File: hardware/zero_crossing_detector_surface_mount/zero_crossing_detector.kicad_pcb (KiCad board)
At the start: 2 copper layers, 93 x 61 mm, 85 parts, among them J1 Conn_01x02, J2 BOOT0, J3 Conn_02x14_Odd_Even, J4 USB_B_Micro, J5 PowerSelect, J6 K-Type, J7 BOOT1, Q1 2N3904, SW1 Reset, U1 EL357N(C)(TA)-G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

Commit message: Added open hardware logo to PCB. Fixed some doc typos
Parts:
- added REF**: OSHW-Symbol_6.7x6mm_SilkScreen, Symbol:OSHW-Symbol_6.7x6mm_SilkScreen, B.Cu at (204.2, 55.9)
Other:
- board text added: "open hardware open software"

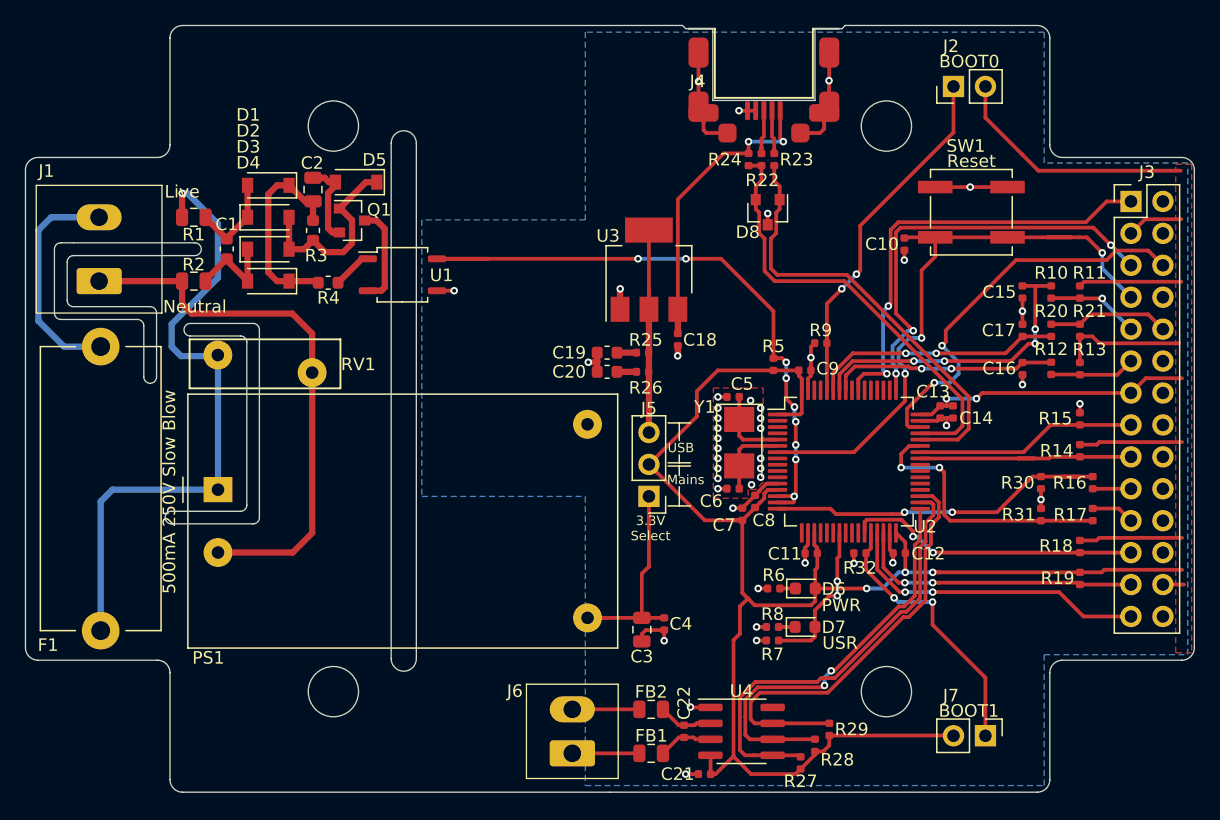
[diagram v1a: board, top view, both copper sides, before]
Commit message: Changed to 5v AC-DC module. Added transistor to drive SSR output. Updated LDO
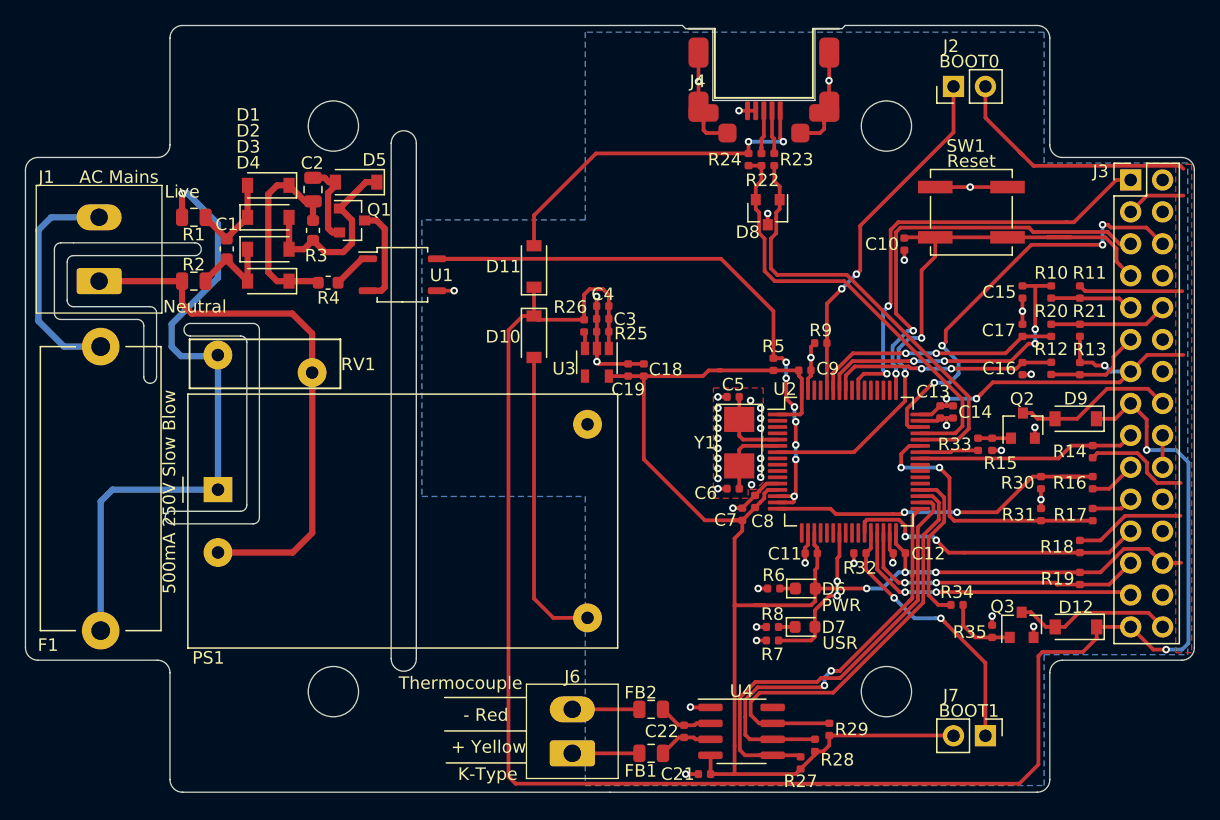
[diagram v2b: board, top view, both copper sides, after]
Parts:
- removed C20: 22uF, Capacitor_SMD:C_0603_1608Metric
- removed J5: PowerSelect, Connector_PinHeader_2.54mm:PinHeader_1x03_P2.54mm_Vertical
- added D10: B5819W, Diode_SMD:D_SOD-123, F.Cu at (204.0, 64.3)
- added D11: B5819W, Diode_SMD:D_SOD-123, F.Cu at (204.0, 58.7)
- added D12: 1N4148, Diode_SMD:D_SOD-123, F.Cu at (247.1, 87.4)
- added D9: 1N4148, Diode_SMD:D_SOD-123, F.Cu at (247.1, 70.8)
- added Q2: 2N3904, Package_TO_SOT_SMD:SOT-23, F.Cu at (242.9, 71.3)
- added Q3: 2N3904, Package_TO_SOT_SMD:SOT-23, F.Cu at (242.8, 87.2)
- added R33: 1k, Resistor_SMD:R_0402_1005Metric, F.Cu at (239.3, 72.8)
- added R34: 1k, Resistor_SMD:R_0402_1005Metric, F.Cu at (237.6, 85.6)
- added R35: 10k, Resistor_SMD:R_0402_1005Metric, F.Cu at (240.4, 87.7)
- C18: value 4.7uf -> 10uF
- C19: value 22uF -> 100nF; footprint Capacitor_SMD:C_0603_1608Metric -> Capacitor_SMD:C_0402_1005Metric
- C3: footprint Capacitor_SMD:C_0805_2012Metric -> Capacitor_SMD:C_0402_1005Metric
- J3: value Conn_02x14_Odd_Even -> Conn_02x15_Odd_Even; footprint Connector_PinHeader_2.54mm:PinHeader_2x14_P2.54mm_Vertical -> Connector_PinHeader_2.54mm:PinHeader_2x15_P2.54mm_Vertical
- PS1: value HLK-PM03 -> HLK-PM01
- R25, R26: value 1 -> 100k
- U3: value AMS1117 -> AP2112K-3.3; footprint Package_TO_SOT_SMD:SOT-223-3_TabPin2 -> Package_TO_SOT_SMD:SOT-23-5
- moved C4 25.8 mm to (209.4, 61.8), turned to 180 degrees
- moved C3 24.9 mm to (209.4, 62.8), turned to 180 degrees
- moved U3 8.45 mm to (209.0, 66.3), turned to 270 degrees
- moved R15 7.27 mm to (240.4, 72.8)
- moved R26 5.92 mm to (207.9, 63.4), turned to 90 degrees
- moved C18 3.63 mm to (212.7, 66.9), turned to 90 degrees
- moved R25 3.58 mm to (209.4, 63.9), turned to 180 degrees
- moved C19 2.17 mm to (211.5, 66.9), turned to 90 degrees
- moved J3 1.71 mm to (251.4, 51.8)
- moved R14 1.02 mm to (248.4, 73.4), turned to 270 degrees
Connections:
- C18 pad 1: /VBUS -> VCC
- C19 pad 1: Net-(C19-Pad1) -> VCC
- C3 pad 1: /3.3V_MAINS -> +5V
- C4 pad 1: /3.3V_MAINS -> +5V
- J3 pad 15: /SSR -> +5V
- J3 pad 16: GND -> /SSR_RAW
- J4 pad 1: /VBUS -> /5V_USB
- PS1 pad 4: /3.3V_MAINS -> /5V_MAINS
- R15 pad 1: /SSR -> GND
- R15 pad 2: GND -> Net-(Q2-Pad1)
- R24 pad 2: /VBUS -> /5V_USB
- R25 pad 1: Net-(C19-Pad1) -> +5V
- R25 pad 2: /3.3V_USB -> GND
- R26 pad 1: Net-(C20-Pad1) -> Net-(R26-Pad1)
- R26 pad 2: /3.3V_USB -> +5V
- U2 pad 36: Net-(U2-Pad36) -> /MISC
- U3 pad 1: GND -> +5V
- U3 pad 2: /3.3V_USB -> GND
- U3 pad 3: /VBUS -> Net-(R26-Pad1)
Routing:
- net +5V: track 0.00 -> 144.6 mm, vias 0 -> 2
- net /5V_USB: track 0.00 -> 27.8 mm, vias 0 -> 2
- net /VBUS: track 24.1 -> 0.00 mm, vias 2 -> 0
- net /5V_MAINS: track 0.00 -> 24.1 mm
- net /3.3V_MAINS: track 17.6 -> 0.00 mm
- net /3.3V_USB: track 16.1 -> 0.00 mm
- net /SSR: track 17.7 -> 4.66 mm
- net /SSR_RAW: track 0.00 -> 12.8 mm
- net /MISC_RAW: track 0.00 -> 12.6 mm
- net /MISC: track 0.00 -> 12.5 mm
- net VCC: track 208.0 -> 217.3 mm, vias 5 -> 6
- net GND: track 63.6 -> 69.4 mm, vias 44 -> 45
- net Net-(Q3-Pad1): track 0.00 -> 5.73 mm
- net Net-(Q2-Pad1): track 0.00 -> 2.62 mm
- net /SWDIO: track 32.2 -> 34.1 mm, vias 2 -> 4
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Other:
- board text added: "+ Yellow"
- board text added: "- Red"
- board text added: "3.3V"
- board text added: "AC Mains"
- board text added: "K-Type"
- board text added: "MISC +"
- board text added: "MISC -"
- board text added: "SSR +"
- board text added: "SSR -"
- board text added: "Thermocouple"
- board text added: "Zero Crossing SSR Controller (SMD) v0.2 oshthings.com/zcssr 13-Nov-19"
- board text removed: "3.3V Select"
- board text removed: "Mains"
- board text removed: "SSR"
- board text removed: "USB"
- board text removed: "Zero Crossing SSR Controller (SMD) v0.2 oshthings.com/zcssr 11-Nov-19"

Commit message: Added some extra silkscreen labels to IO. Fixed image links in project log
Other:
- board text added: "(3.3V)"
- board text added: "(5V)"
- board text added: "(Active LOW)"
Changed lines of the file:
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@@
   (general
     (thickness 1.6)
-    (drawings 141)
+    (drawings 146)
     (tracks 795)
     (zones 0)
@@
     (pad "" np_thru_hole circle (at 0 0) (size 4 4) (drill 4) (layers *.Cu *.Mask))
   )
+  (gr_text "(3.3V)" (at 238.506 84.836) (layer B.SilkS)
+    (effects (font (size 0.75 0.75) (thickness 0.1)) (justify left mirror))
+  )
+  (gr_text "(3.3V)" (at 238.506 82.296) (layer B.SilkS)
+    (effects (font (size 0.75 0.75) (thickness 0.1)) (justify left mirror))
+  )
+  (gr_text "(Active LOW)" (at 238.506 72.136) (layer B.SilkS)
+    (effects (font (size 0.75 0.75) (thickness 0.1)) (justify left mirror))
+  )
+  (gr_text "(5V)" (at 238.506 69.596) (layer B.SilkS)
+    (effects (font (size 0.75 0.75) (thickness 0.1)) (justify left mirror))
+  )
+  (gr_text "(5V)" (at 238.506 87.376) (layer B.SilkS)
+    (effects (font (size 0.75 0.75) (thickness 0.1)) (justify left mirror))
+  )
   (gr_text "AC Mains" (at 170.942 51.562) (layer F.SilkS)

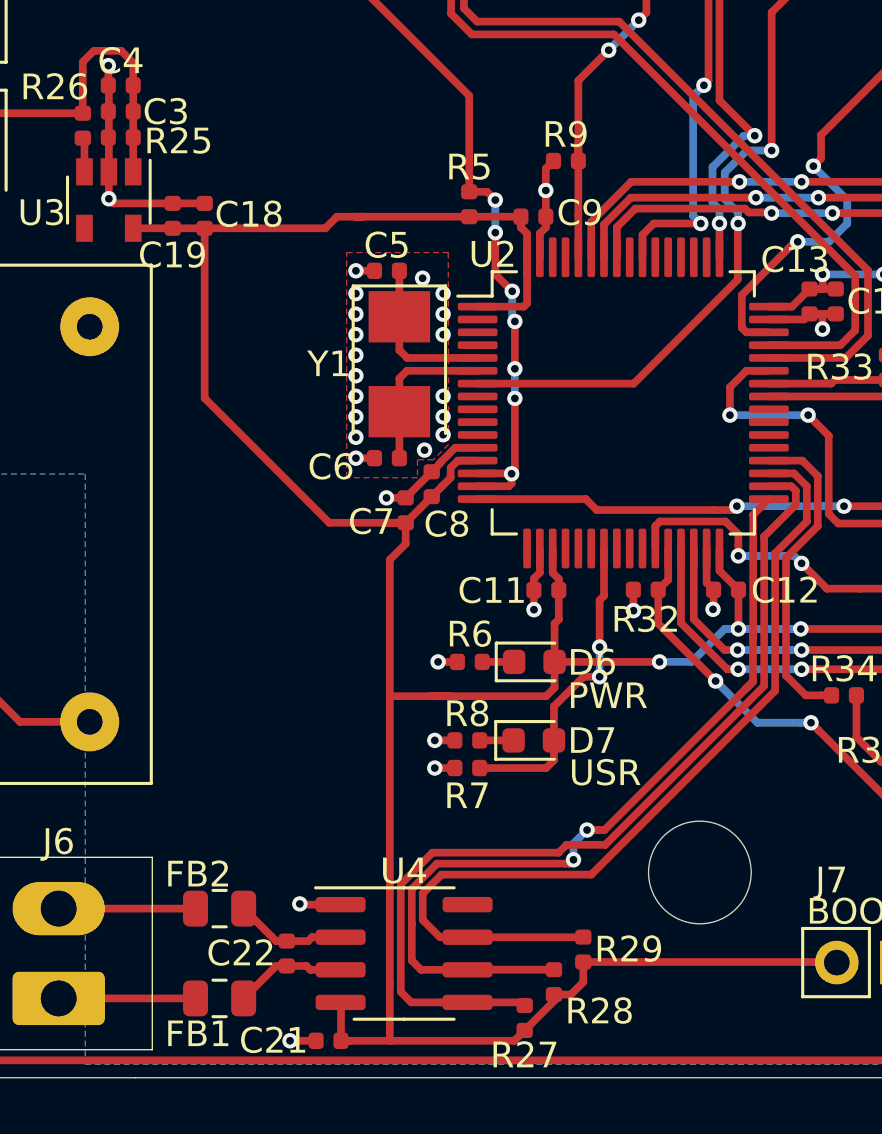
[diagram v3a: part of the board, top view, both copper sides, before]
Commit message: Added tiny 1x1mm RGB LED to pcb
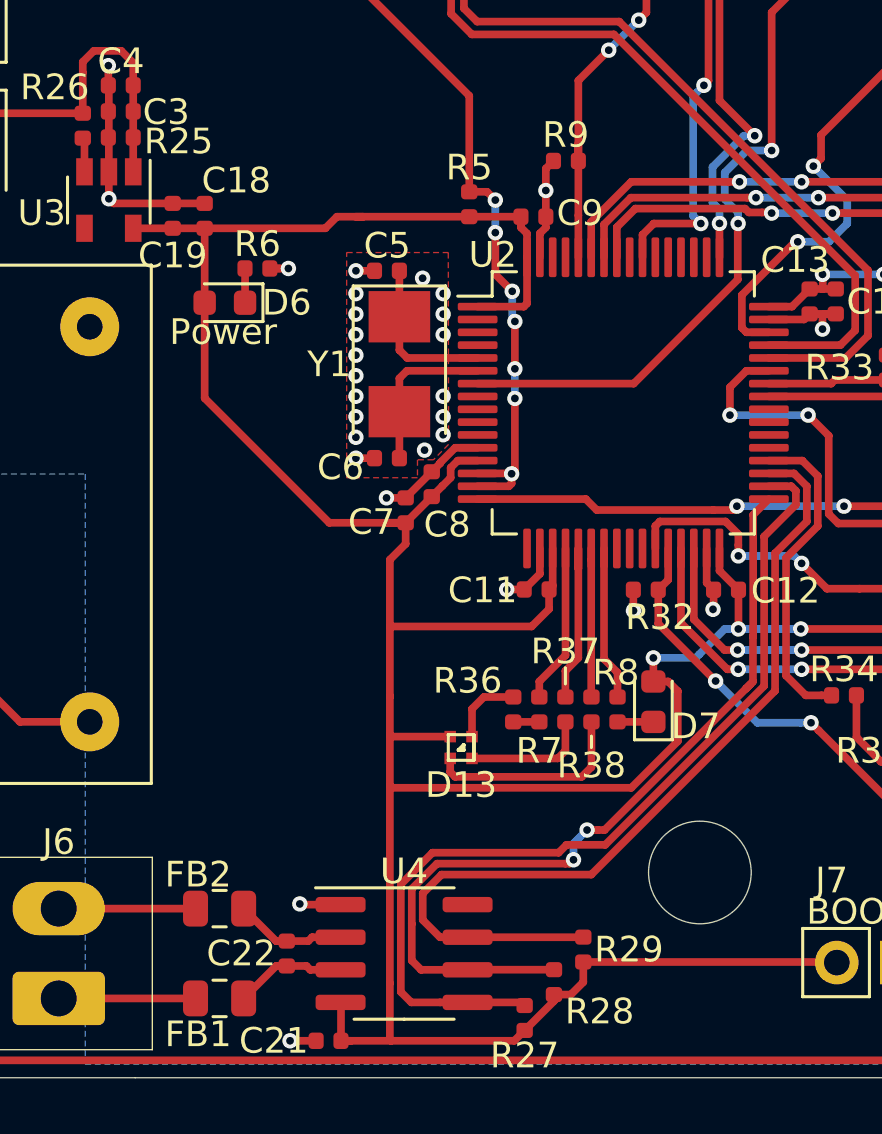
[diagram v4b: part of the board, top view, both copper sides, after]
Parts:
- added D13: LED_ARBG, Custom:SMLP34RGB, F.Cu at (222.7, 87.6)
- added R36: 220, Resistor_SMD:R_0402_1005Metric, F.Cu at (224.7, 86.1)
- added R37: 75, Resistor_SMD:R_0402_1005Metric, F.Cu at (226.8, 86.1)
- added R38: 47, Resistor_SMD:R_0402_1005Metric, F.Cu at (227.8, 86.1)
- R7: value 10k -> 33
- R8: value 150 -> 220
- moved D6 18.5 mm to (213.5, 70.3), turned to 180 degrees
- moved R6 17.4 mm to (214.8, 69.0), turned to 0 degrees
- moved R8 5.98 mm to (228.8, 86.1), turned to 90 degrees
- moved D7 4.90 mm to (230.2, 85.8), turned to 90 degrees
- moved R7 3.62 mm to (225.7, 86.1), turned to 90 degrees
- moved C11 0.38 mm to (225.6, 81.5)
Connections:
- D7 pad 2: /USR_LED -> VCC
- R7 pad 1: /USR_LED -> Net-(R36-Pad2)
- R7 pad 2: GND -> /R_LED
- R8 pad 2: GND -> /USR_LED
- U2 pad 20: Net-(U2-Pad20) -> /R_LED
- U2 pad 21: Net-(U2-Pad21) -> /B_LED
- U2 pad 22: Net-(U2-Pad22) -> /G_LED
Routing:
- net VCC: track 217.3 -> 227.5 mm
- net Net-(D13-Pad4): track 0.00 -> 8.03 mm
- net /B_LED: track 0.00 -> 6.77 mm
- net /USR_LED: track 12.4 -> 6.01 mm, vias 2 -> 0
- net /R_LED: track 0.00 -> 6.21 mm
- net /G_LED: track 0.00 -> 5.79 mm
- net Net-(D13-Pad3): track 0.00 -> 4.89 mm
- net Net-(D13-Pad2): track 0.00 -> 2.88 mm
- net GND: track 69.4 -> 68.3 mm, vias 45 -> 43
- net Net-(R36-Pad2): track 0.00 -> 1.02 mm
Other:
- board text added: "Power"
- board text added: "Zero Crossing SSR Controller (SMD) v0.2 oshthings.com/zcssr 15-Nov-19"
- board text removed: "PWR"
- board text removed: "USR"
- board text removed: "Zero Crossing SSR Controller (SMD) v0.2 oshthings.com/zcssr 13-Nov-19"

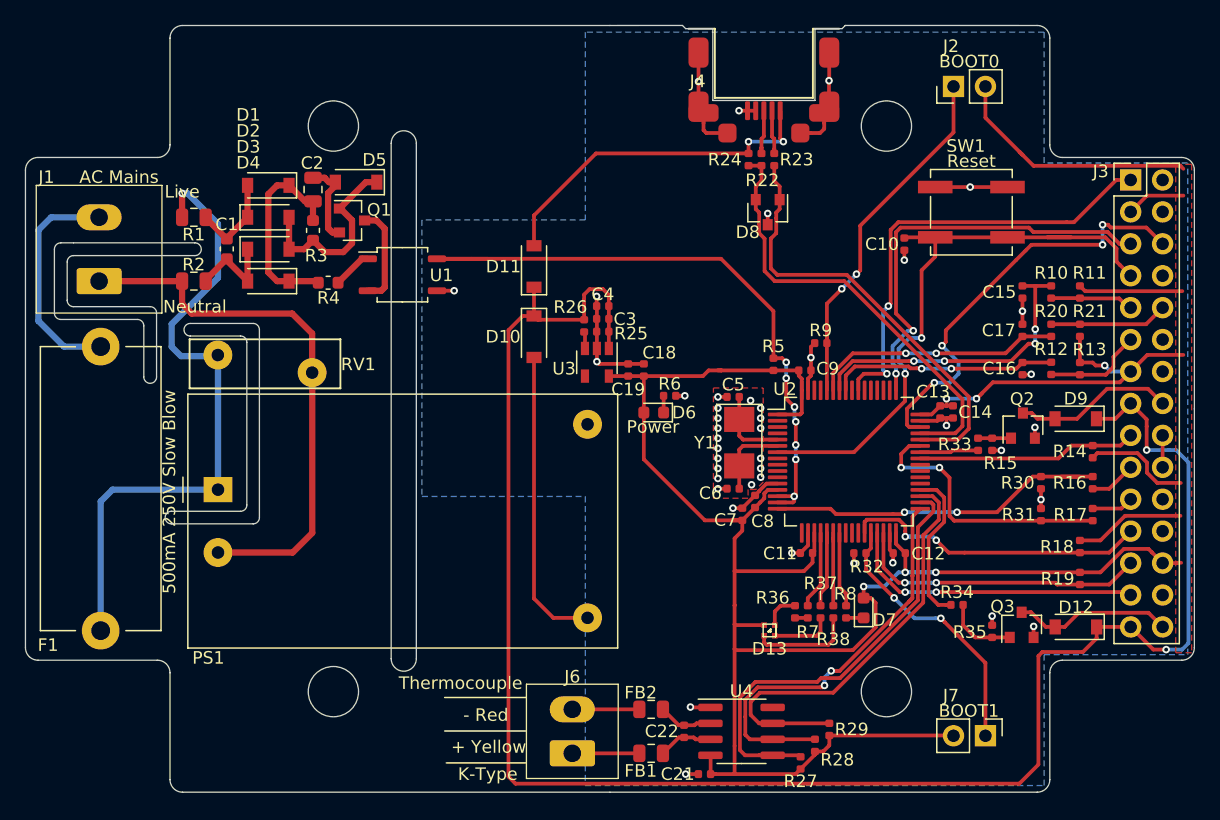
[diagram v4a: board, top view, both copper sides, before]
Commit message: Switched USB ESD diode for STM recommened one. Added GND plane around USB traces on top layer
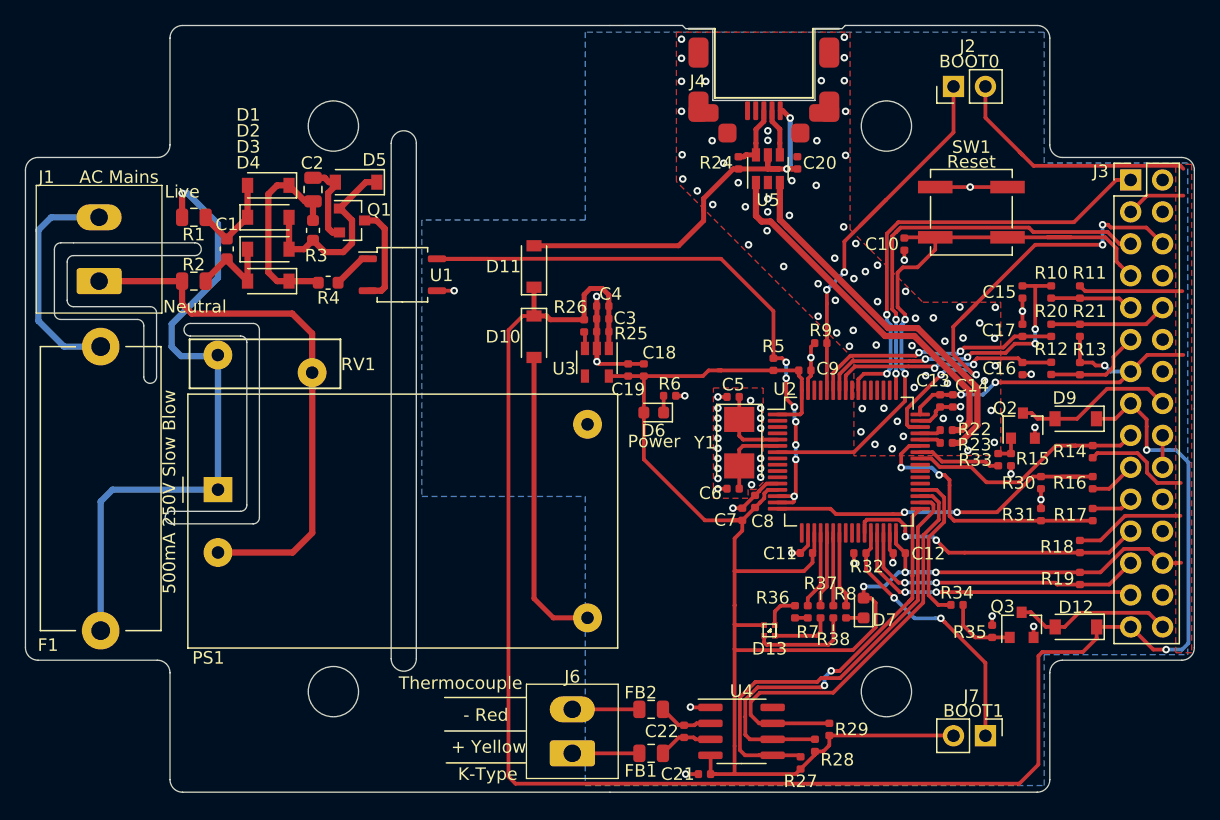
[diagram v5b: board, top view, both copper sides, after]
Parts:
- removed D8: CESD5V0AP, Package_TO_SOT_SMD:SOT-23
- added C20: 100nF, Capacitor_SMD:C_0402_1005Metric, F.Cu at (224.9, 50.4)
- added U5: USBLC6-2SC6, Package_TO_SOT_SMD:SOT-23-6, F.Cu at (222.6, 50.9)
- moved R23 26.4 mm to (236.8, 72.7), turned to 0 degrees
- moved R22 26.1 mm to (236.8, 71.7), turned to 0 degrees
- moved R33 2.01 mm to (240.9, 74.0)
- moved R15 1.93 mm to (241.9, 74.0)
- moved C13 0.88 mm to (236.3, 69.4)
- moved C14 0.88 mm to (237.3, 69.4)
- moved R24 0.84 mm to (220.2, 50.4), turned to 270 degrees
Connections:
- R22 pad 2: /D+ -> Net-(R22-Pad2)
- R23 pad 2: /D- -> Net-(R23-Pad2)
- R24 pad 1: /USBD+ -> /D+
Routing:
- net /USBD+: track 35.6 -> 1.70 mm
- net /USBD-: track 35.4 -> 1.70 mm
- net Net-(R22-Pad2): track 0.00 -> 32.1 mm
- net Net-(R23-Pad2): track 0.00 -> 29.8 mm
- net GND: track 68.3 -> 54.9 mm, vias 43 -> 110
- net /5V_USB: track 27.8 -> 31.9 mm
- net /SWDIO: track 34.1 -> 37.1 mm
- net /BOOT0: track 29.0 -> 32.0 mm
- net /SSR: track 4.66 -> 6.65 mm
- net /Trigger: track 17.5 -> 19.4 mm
- net /D+: track 3.75 -> 5.22 mm
- net /SWNRST: track 48.6 -> 49.2 mm
- net /SWCLK: track 33.6 -> 33.0 mm
